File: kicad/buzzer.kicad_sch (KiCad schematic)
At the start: 1 part

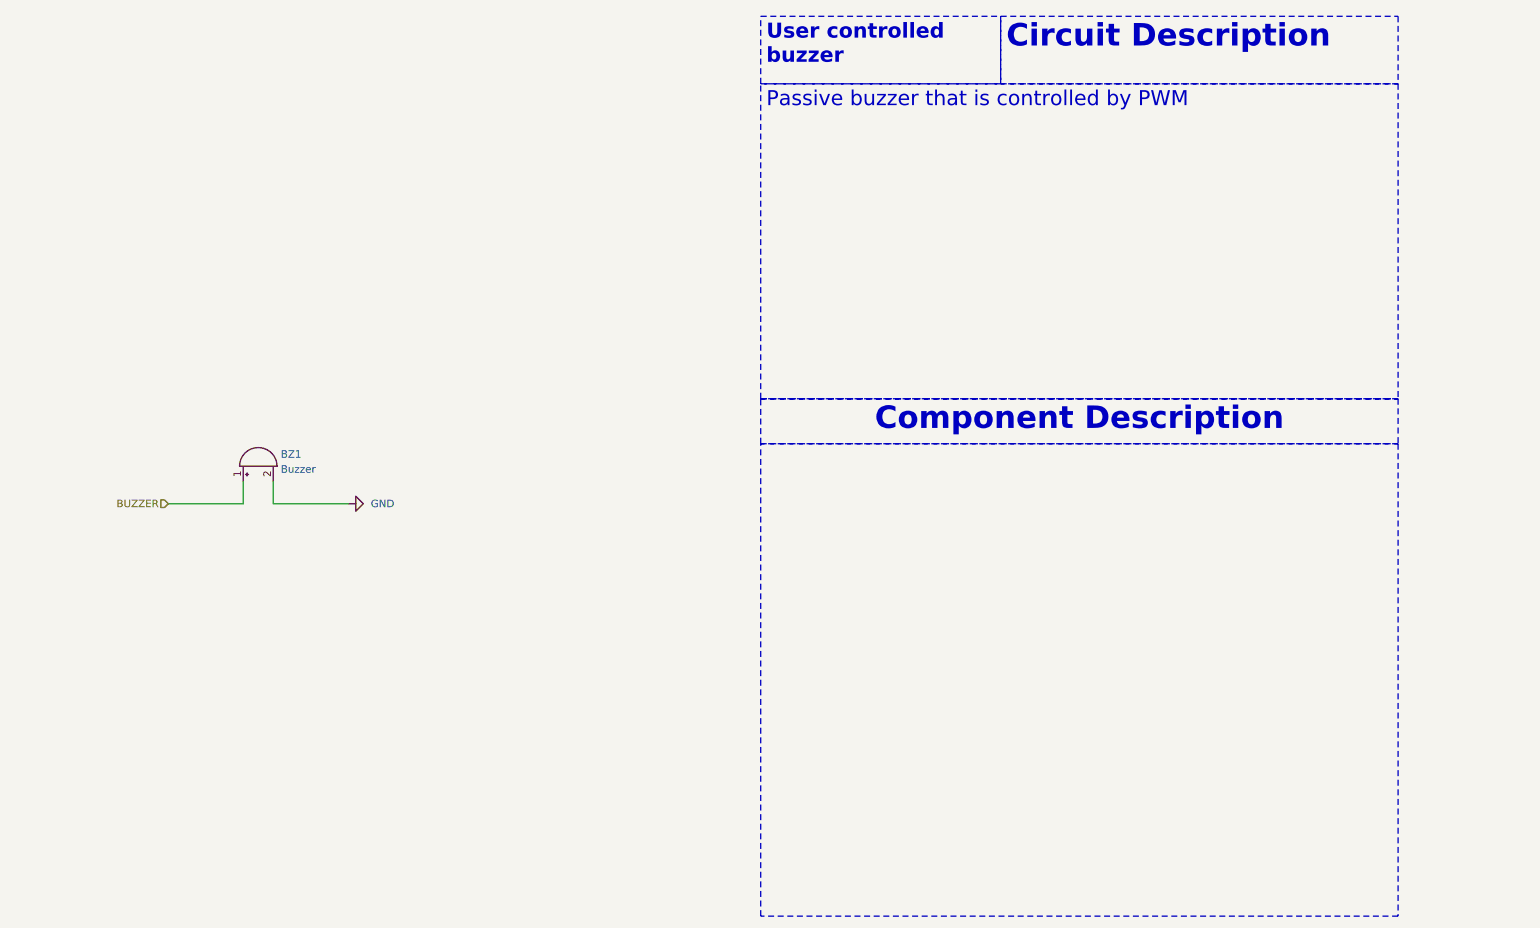
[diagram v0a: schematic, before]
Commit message: feat: replace placeholder buzzer circuit with final circuit
Signed-off-by: Bobo Bäck Engström <bobo@id8-engineering.io>
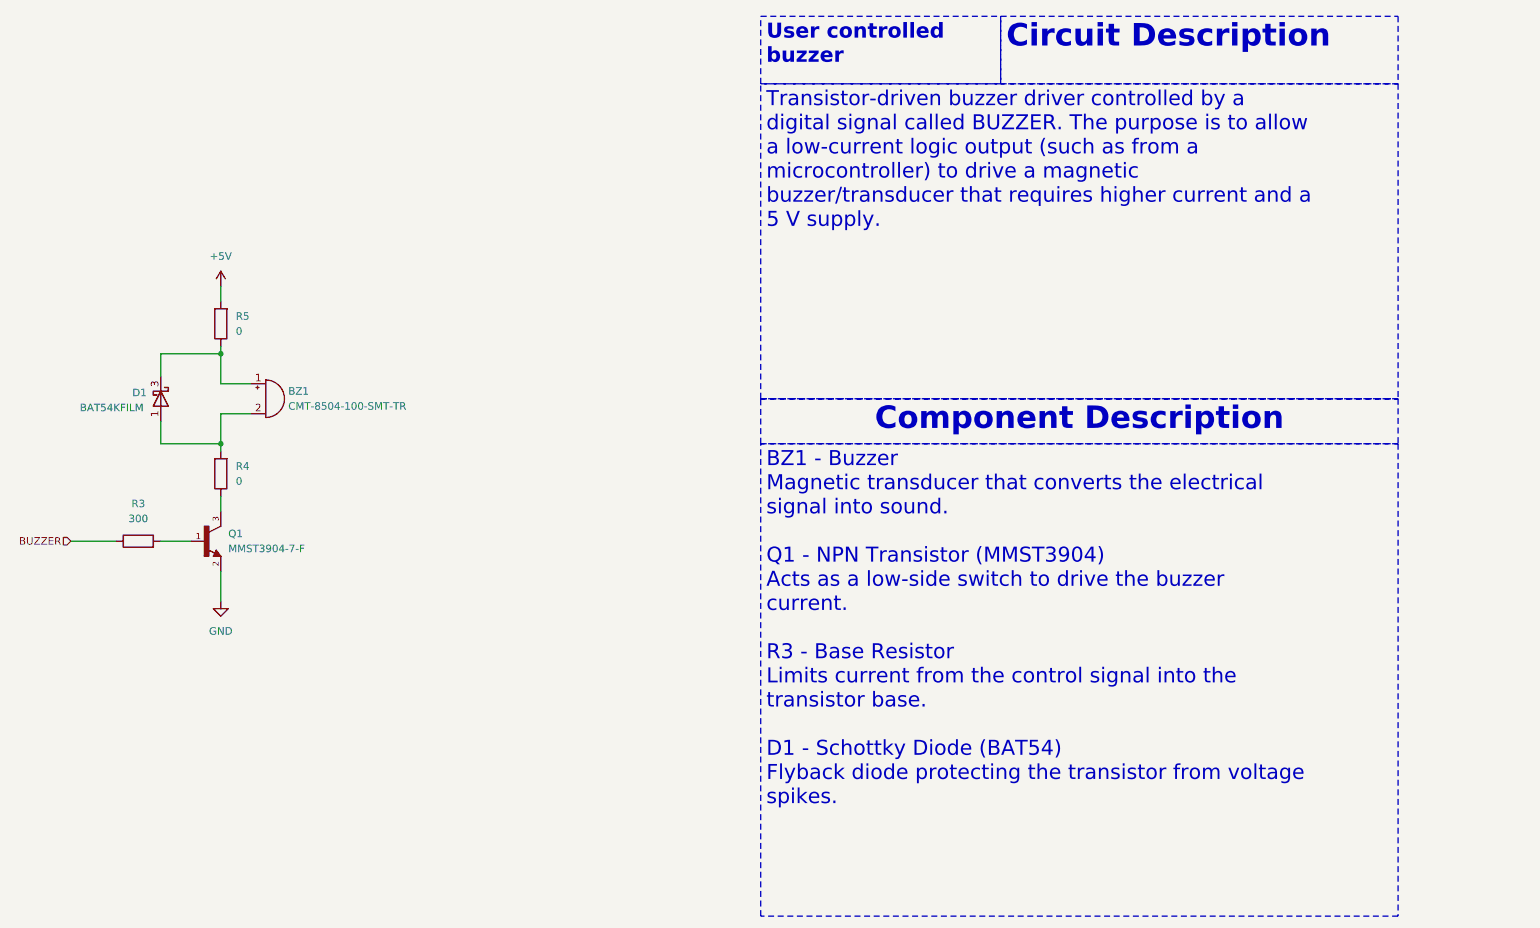
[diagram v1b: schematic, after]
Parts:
- added D1: BAT54KFILM, seven-lib:D_SOD-523, symbol seven_lib:BAT54W
- added Q1: MMST3904-7-F, seven-lib:SOT65P210X110-3N, symbol seven_lib:MMST3904-7-F
- added R3: 300, seven-lib:R_0603_1608Metric, symbol seven_lib:R
- added R4, R5: 0, seven-lib:R_0603_1608Metric, symbol seven_lib:R
- BZ1: value Buzzer -> CMT-8504-100-SMT-TR; footprint (none) -> seven-lib:XDCR_CMT-8504-100-SMT-TR
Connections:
- net BUZZER: now also R3.1; no longer BZ1.1 (+)
- net GND: now also Q1.2; no longer BZ1.2 (-)
- new net: BZ1.1 (+), D1.3 (K), R5.1
- new net: Q1.3, R4.1
- new net: BZ1.2 (-), D1.1 (A), R4.2
- new net: Q1.1, R3.2
- new net +5V: R5.2

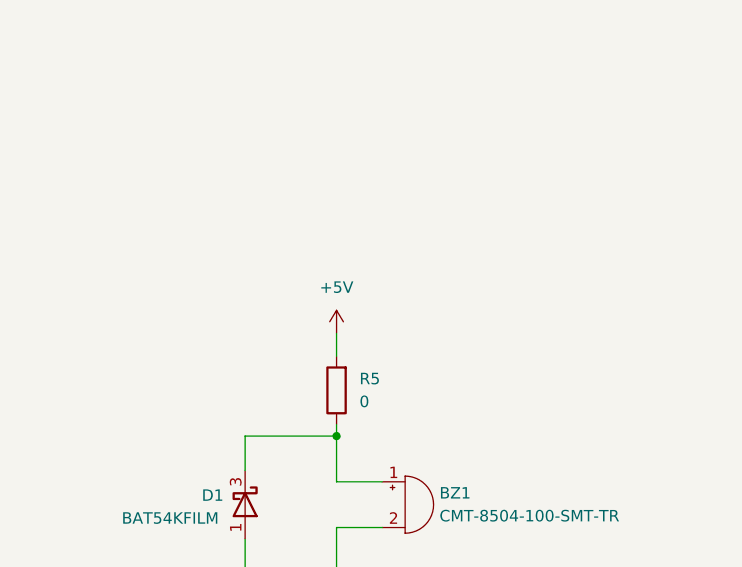
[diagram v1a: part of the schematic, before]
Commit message: feat: remake power management and use the same as the reference DK
Signed-off-by: Bobo Bäck Engström <bobo@id8-engineering.io>
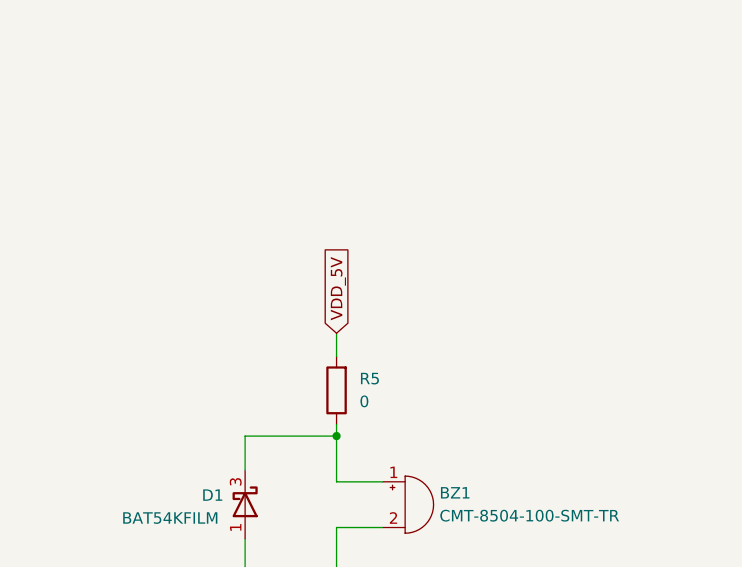
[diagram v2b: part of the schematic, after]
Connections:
- net +5V renamed VDD_5V
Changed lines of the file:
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@@
+		)
+	)
+	(global_label "VDD_5V"
+		(shape input)
+		(at 85.09 58.42 90)
+		(fields_autoplaced yes)
+		(effects
+			(font
+				(size 1.27 1.27)
+			)
+			(justify left)
+		)
+		(property "Intersheetrefs" "${INTERSHEET_REFS}"
+			(at 85.09 48.5405 90)
+			(effects
+				(font
+					(size 1.27 1.27)
+				)
+				(justify left)
+				(hide yes)
+			)
 		)
 	)
@@
 					(unit 1)
 				)
-			)
-		)
-	)
-	(symbol
-		(lib_id "seven_lib:+5V")
-		(at 85.09 58.42 0)
-		(unit 1)
-		(exclude_from_sim no)
-		(in_bom yes)
-		(on_board yes)
-		(dnp no)
-		(fields_autoplaced yes)
-		(property "Reference" "#PWR023"
-			(at 85.09 62.23 0)
-			(effects
-				(font
-					(size 1.27 1.27)
-				)
-				(hide yes)
-			)
-		)
-		(property "Value" "+5V"
-			(at 85.09 53.34 0)
-			(effects
-				(font
-					(size 1.27 1.27)
-				)
-			)
-		)
-		(property "Footprint" ""
-			(at 85.09 58.42 0)
-			(effects
-				(font
-					(size 1.27 1.27)
-				)
-				(hide yes)
-			)
-		)
-		(property "Datasheet" ""
-			(at 85.09 58.42 0)
-			(effects
-				(font
-					(size 1.27 1.27)
-				)
-				(hide yes)
-			)
-		)
-		(property "Description" "Power symbol creates a global label with name \"+5V\""
-			(at 85.09 58.42 0)
-			(effects
-				(font
-					(size 1.27 1.27)
-				)
-				(hide yes)
-			)
-		)
-		(pin "1"
-		)
-		(instances
-			(project ""
-				(path "/8e3cc843-5797-49f3-8b3a-1c11450ccd1e/3959a5c9-da67-4dbd-8c3b-230c0962e71e"
-					(reference "#PWR023")
-					(unit 1)
-				)

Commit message: fix: change R fp to a smaller one
Signed-off-by: Bobo Bäck Engström <bobo@id8-engineering.io>
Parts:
- R3, R4, R5: footprint seven-lib:R_0603_1608Metric -> seven-lib:R_0402_1005Metric
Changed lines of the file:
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@@
 			)
 		)
-		(property "Footprint" "seven-lib:R_0603_1608Metric"
+		(property "Footprint" "seven-lib:R_0402_1005Metric"
 			(at 86.868 64.77 90)
 			(effects
@@
 			)
 		)
-		(property "Footprint" "seven-lib:R_0603_1608Metric"
+		(property "Footprint" "seven-lib:R_0402_1005Metric"
 			(at 86.868 90.17 90)
 			(effects
@@
 			)
 		)
-		(property "Footprint" "seven-lib:R_0603_1608Metric"
+		(property "Footprint" "seven-lib:R_0402_1005Metric"
 			(at 71.12 103.378 90)
 			(effects

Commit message: fix: changes made according to review meeting
Signed-off-by: Bobo Bäck Engström <bobo@id8-engineering.io>
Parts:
- added TP12: BUZZER, seven-lib:TestPoint_Pad_2.0x2.0mm, symbol seven_lib:TestPoint
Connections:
- net BUZZER: now also TP12.1
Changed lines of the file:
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@@
+	)
+	(junction
+		(at 64.77 101.6)
+		(diameter 0)
+		(color 0 0 0 0)
 	)
 	(junction
@@
 	(wire
 		(pts
-			(xy 59.69 101.6) (xy 67.31 101.6)
+			(xy 59.69 101.6) (xy 64.77 101.6)
+		)
+		(stroke
+			(width 0)
+			(type default)
+		)
+	)
+	(wire
+		(pts
+			(xy 64.77 104.14) (xy 64.77 101.6)
 		)
 		(stroke
@@
 			(width 0)
 			(type dash)
+		)
+	)
+	(wire
+		(pts
+			(xy 64.77 101.6) (xy 67.31 101.6)
+		)
+		(stroke
+			(width 0)
+			(type default)
 		)
 	)
@@
 					(unit 1)
 				)
+			)
+		)
+	)
+	(symbol
+		(lib_id "seven_lib:TestPoint")
+		(at 64.77 104.14 180)
+		(unit 1)
+		(exclude_from_sim no)
+		(in_bom yes)
+		(on_board yes)
+		(dnp no)
+		(property "Reference" "TP12"
+			(at 60.833 106.045 0)
+			(effects
+				(font
+					(size 1.27 1.27)
+				)
+			)
+		)
+		(property "Value" "BUZZER"
+			(at 60.833 108.585 0)
+			(effects
+				(font
+					(size 1.27 1.27)
+				)
+			)
+		)
+		(property "Footprint" "seven-lib:TestPoint_Pad_2.0x2.0mm"
+			(at 59.69 104.14 0)
+			(effects
+				(font
+					(size 1.27 1.27)
+				)
+				(hide yes)
+			)
+		)
+		(property "Datasheet" "~"
+			(at 59.69 104.14 0)
+			(effects
+				(font
+					(size 1.27 1.27)
+				)
+				(hide yes)
+			)
+		)
+		(property "Description" "test point"
+			(at 64.77 104.14 0)
+			(effects
+				(font
+					(size 1.27 1.27)
+				)
+				(hide yes)
+			)
+		)
+		(pin "1"
+		)
+		(instances
+			(project "seven"
+				(path "/8e3cc843-5797-49f3-8b3a-1c11450ccd1e/3959a5c9-da67-4dbd-8c3b-230c0962e71e"
+					(reference "TP12")
+					(unit 1)
+				)

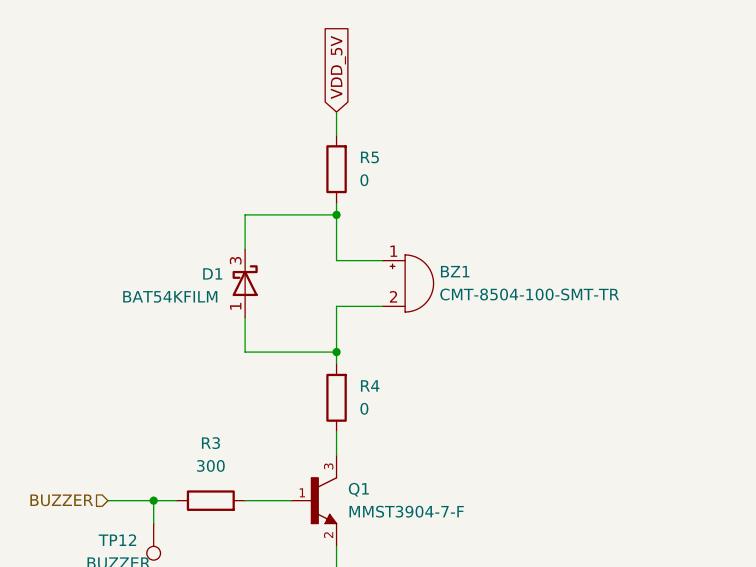
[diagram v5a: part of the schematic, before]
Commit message: fix: satisfy warnings in pcb
Signed-off-by: Bobo Bäck Engström <bobo@id8-engineering.io>
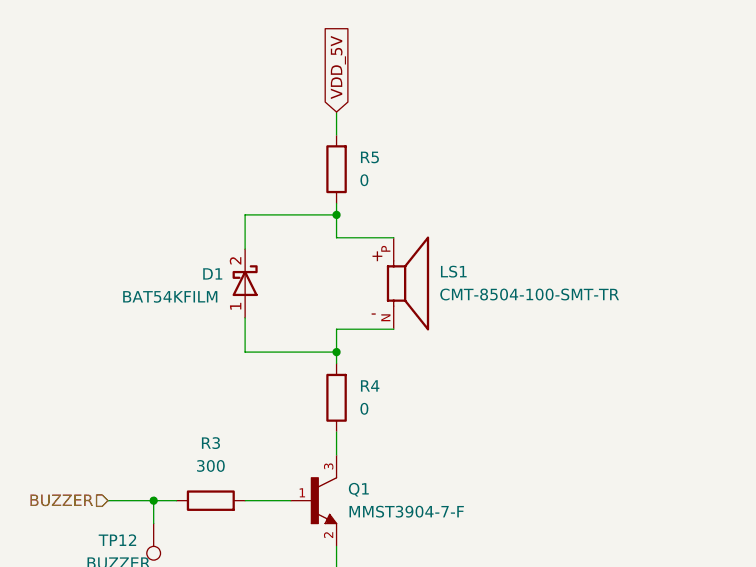
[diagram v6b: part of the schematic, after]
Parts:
- removed BZ1: CMT-8504-100-SMT-TR, seven-lib:XDCR_CMT-8504-100-SMT-TR, symbol seven_lib:Buzzer
- added LS1: CMT-8504-100-SMT-TR, seven-lib:XDCR_CMT-8504-100-SMT-TR, symbol seven_lib:CMT-8504-100-SMT-TR
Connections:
- net at R5.1: now also D1.2 (K), LS1.P; no longer D1.3 (K)
- net at D1.1 (A), R4.2: now also LS1.N
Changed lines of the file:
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@@
+	(wire
+		(pts
+			(xy 85.09 69.85) (xy 85.09 72.39)
+		)
+		(stroke
+			(width 0)
+			(type default)
+		)
+	)
 	(wire
 		(pts
@@
 		)
 	)
-	(wire
-		(pts
-			(xy 85.09 80.01) (xy 90.17 80.01)
-		)
-		(stroke
-			(width 0)
-			(type default)
-		)
-	)
 	(polyline
 		(pts
@@
 	(wire
 		(pts
+			(xy 85.09 72.39) (xy 91.44 72.39)
+		)
+		(stroke
+			(width 0)
+			(type default)
+		)
+	)
+	(wire
+		(pts
 			(xy 74.93 101.6) (xy 80.01 101.6)
 		)
@@
 	(wire
 		(pts
+			(xy 85.09 68.58) (xy 85.09 69.85)
+		)
+		(stroke
+			(width 0)
+			(type default)
+		)
+	)
+	(wire
+		(pts
 			(xy 85.09 106.68) (xy 85.09 111.76)
 		)
@@
 	(wire
 		(pts
-			(xy 85.09 74.93) (xy 90.17 74.93)
-		)
-		(stroke
-			(width 0)
-			(type default)
-		)
-	)
-	(wire
-		(pts
 			(xy 74.93 69.85) (xy 74.93 73.66)
 		)
@@
 	(wire
 		(pts
-			(xy 85.09 85.09) (xy 85.09 80.01)
-		)
-		(stroke
-			(width 0)
-			(type default)
-		)
-	)
-	(wire
-		(pts
 			(xy 85.09 69.85) (xy 74.93 69.85)
 		)
@@
 	(wire
 		(pts
-			(xy 85.09 68.58) (xy 85.09 69.85)
-		)
-		(stroke
-			(width 0)
-			(type default)
-		)
-	)
-	(wire
-		(pts
-			(xy 85.09 69.85) (xy 85.09 74.93)
-		)
-		(stroke
-			(width 0)
-			(type default)
-		)
-	)
-	(wire
-		(pts
 			(xy 74.93 85.09) (xy 85.09 85.09)
 		)
@@
 		(pts
 			(xy 85.09 58.42) (xy 85.09 60.96)
+		)
+		(stroke
+			(width 0)
+			(type default)
+		)
+	)
+	(wire
+		(pts
+			(xy 85.09 82.55) (xy 91.44 82.55)
+		)
+		(stroke
+			(width 0)
+			(type default)
+		)
+	)
+	(wire
+		(pts
+			(xy 85.09 85.09) (xy 85.09 82.55)
 		)
 		(stroke
@@
 	)
 	(symbol
+		(lib_id "seven_lib:CMT-8504-100-SMT-TR")
+		(at 91.44 77.47 0)
+		(unit 1)
+		(exclude_from_sim no)
+		(in_bom yes)
+		(on_board yes)
+		(dnp no)
+		(fields_autoplaced yes)
+		(property "Reference" "LS1"
+			(at 96.52 76.1999 0)
+			(effects
+				(font
+					(size 1.27 1.27)
+				)
+				(justify left)
+			)
+		)
+		(property "Value" "CMT-8504-100-SMT-TR"
+			(at 96.52 78.7399 0)
+			(effects
+				(font
+					(size 1.27 1.27)
+				)
+				(justify left)
+			)
+		)
+		(property "Footprint" "seven-lib:XDCR_CMT-8504-100-SMT-TR"
+			(at 91.44 77.47 0)
+			(effects
+				(font
+					(size 1.27 1.27)
+				)
+				(justify bottom)
+				(hide yes)
+			)
+		)
+		(property "Datasheet" "https://eu.mouser.com/datasheet/3/6118/1/cmt_8504_100_smt_tr.pdf"
+			(at 91.44 77.47 0)
+			(effects
+				(font
+					(size 1.27 1.27)
+				)
+				(hide yes)
+			)
+		)
+		(property "Description" ""
+			(at 91.44 77.47 0)
+			(effects
+				(font
+					(size 1.27 1.27)
+				)
+				(hide yes)
+			)
+		)
+		(property "MF" "Same Sky"
+			(at 91.44 77.47 0)
+			(effects
+				(font
+					(size 1.27 1.27)
+				)
+				(justify bottom)
+				(hide yes)
+			)
+		)
+		(property "MAXIMUM_PACKAGE_HEIGHT" "4.00mm"
+			(at 91.44 77.47 0)
+			(effects
+				(font
+					(size 1.27 1.27)
+				)
+				(justify bottom)
+				(hide yes)
+			)
+		)
+		(property "Package" "Package"
+			(at 91.44 77.47 0)
+			(effects
+				(font
+					(size 1.27 1.27)
+				)
+				(justify bottom)
+				(hide yes)
+			)
+		)
+		(property "Price" "None"
+			(at 91.44 77.47 0)
+			(effects
+				(font
+					(size 1.27 1.27)
+				)
+				(justify bottom)
+				(hide yes)
+			)
+		)
+		(property "Check_prices" "https://www.snapeda.com/parts/CMT-8504-100-SMT-TR/Same+Sky/view-part/?ref=eda"
+			(at 91.44 77.47 0)
+			(effects
+				(font
+					(size 1.27 1.27)
+				)
+				(justify bottom)
+				(hide yes)
+			)
+		)
+		(property "STANDARD" "Manufacturer Recommendations"
+			(at 91.44 77.47 0)
+			(effects
+				(font
+					(size 1.27 1.27)
+				)
+				(justify bottom)
+				(hide yes)
+			)
+		)
+		(property "PARTREV" "1.0"
+			(at 91.44 77.47 0)
+			(effects
+				(font
+					(size 1.27 1.27)
+				)
+				(justify bottom)
+				(hide yes)
+			)
+		)
+		(property "SnapEDA_Link" "https://www.snapeda.com/parts/CMT-8504-100-SMT-TR/Same+Sky/view-part/?ref=snap"
+			(at 91.44 77.47 0)
+			(effects
+				(font
+					(size 1.27 1.27)
+				)
+				(justify bottom)
+				(hide yes)
+			)
+		)
+		(property "MP" "CMT-8504-100-SMT-TR"
+			(at 91.44 77.47 0)
+			(effects
+				(font
+					(size 1.27 1.27)
+				)
+				(justify bottom)
+				(hide yes)
+			)
+		)
+		(property "Purchase-URL" "https://www.snapeda.com/api/url_track_click_mouser/?unipart_id=3662542&manufacturer=Same Sky&part_name=CMT-8504-100-SMT-TR&search_term=None"
+			(at 91.44 77.47 0)
+			(effects
+				(font
+					(size 1.27 1.27)
+				)
+				(justify bottom)
+				(hide yes)
+			)
+		)
+		(property "Description_1" "8.5 mm, 5 Vo-p, 100 dB, Surface Mount (SMT), Magnetic Audio Transducer Buzzer"
+			(at 91.44 77.47 0)
+			(effects
+				(font
+					(size 1.27 1.27)
+				)
+				(justify bottom)
+				(hide yes)
+			)
+		)
+		(property "Availability" "In Stock"
+			(at 91.44 77.47 0)
+			(effects
+				(font
+					(size 1.27 1.27)
+				)
+				(justify bottom)
+				(hide yes)
+			)
+		)
+		(property "MANUFACTURER" "CUI Inc."
+			(at 91.44 77.47 0)
+			(effects
+				(font
+					(size 1.27 1.27)
+				)
+				(justify bottom)
+				(hide yes)
+			)
+		)
+		(pin "P"
+		)
+		(pin "N"
+		)
+		(instances
+			(project ""
+				(path "/8e3cc843-5797-49f3-8b3a-1c11450ccd1e/3959a5c9-da67-4dbd-8c3b-230c0962e71e"
+					(reference "LS1")
+					(unit 1)
+				)
+			)
+		)
+	)
+	(symbol
 		(lib_id "seven_lib:R")
 		(at 85.09 90.17 180)
@@
 		(pin "2"
 		)
-		(pin "3"
-		)
 		(pin "1"
 		)
@@
 					(unit 1)
 				)
-			)
-		)
-	)
-	(symbol
-		(lib_id "seven_lib:Buzzer")
-		(at 92.71 77.47 0)
-		(unit 1)
-		(exclude_from_sim no)
-		(in_bom yes)
-		(on_board yes)
-		(dnp no)
-		(fields_autoplaced yes)
-		(property "Reference" "BZ1"
-			(at 96.52 76.1999 0)
-			(effects
-				(font
-					(size 1.27 1.27)
-				)
-				(justify left)
-			)
-		)
-		(property "Value" "CMT-8504-100-SMT-TR"
-			(at 96.52 78.7399 0)
-			(effects
-				(font
-					(size 1.27 1.27)
-				)
-				(justify left)
-			)
-		)
-		(property "Footprint" "seven-lib:XDCR_CMT-8504-100-SMT-TR"
-			(at 92.075 74.93 90)
-			(effects
-				(font
-					(size 1.27 1.27)
-				)
-				(hide yes)
-			)
-		)
-		(property "Datasheet" "https://eu.mouser.com/datasheet/3/6118/1/cmt_8504_100_smt_tr.pdf"
-			(at 92.075 74.93 90)
-			(effects
-				(font
-					(size 1.27 1.27)
-				)
-				(hide yes)
-			)
-		)
-		(property "Description" "Buzzer, polarized"
-			(at 92.71 77.47 0)
-			(effects
-				(font
-					(size 1.27 1.27)
-				)
-				(hide yes)
-			)
-		)
-		(pin "2"
-		)
-		(pin "1"
-		)
-		(instances
-			(project ""
-				(path "/8e3cc843-5797-49f3-8b3a-1c11450ccd1e/3959a5c9-da67-4dbd-8c3b-230c0962e71e"
-					(reference "BZ1")
-					(unit 1)
-				)
